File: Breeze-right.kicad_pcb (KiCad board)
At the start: 2 copper layers, 210.6 x 114.9 mm, 103 parts, among them J1 J, SW1 CHOCXHSPCB-1U, SW10 CHOCXHSPCB-1U, SW11 CHOCXHSPCB-1U, SW12 CHOCXHSPCB-1U, SW13 CHOCXHSPCB-1U, SW14 CHOCXHSPCB-1U, SW15 CHOCXHSPCB-1U, SW16 CHOCXHSPCB-1U, SW17 CHOCXHSPCB-1U, SW18 CHOCXHSPCB-1U, SW19 CHOCXHSPCB-1U, SW2 CHOCXHSPCB-1U, SW20 CHOCXHSPCB-1U, SW21 CHOCXHSPCB-1U, SW22 CHOCXHSPCB-1U, SW23 CHOCXHSPCB-1U, SW24 CHOCXHSPCB-1U, SW3 CHOCXHSPCB-1U, SW4 CHOCXHSPCB-1U, SW5 CHOCXHSPCB-1U, SW6 CHOCXHSPCB-1U, SW7 CHOCXHSPCB-1U, SW8 CHOCXHSPCB-1U, SW9 CHOCXHSPCB-1U

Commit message: done
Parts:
- removed H15: 2M-HOLE, Breeze:M2-HOLE
- removed H16, H17, H19: M3-HOLE, Breeze:M3-HOLE
- removed the H18 at (193.9, 114.4)
- removed MCU-MAIN1: PRO-MICRO, Breeze:ProMicro_1-Sided
- removed PWR1: SW_SPDT, Breeze:SS12D00
- added H12: M3, MountingHole:MountingHole_3.2mm_M3_ISO7380_Pad, F.Cu at (294.1, 120.3)
- added H14: M3, MountingHole:MountingHole_3.2mm_M3_ISO7380_Pad, F.Cu at (294.2, 158.2)
- added SW1: SW_SPDT, Breeze:SS12D00, F.Cu at (125.8, 167.5)
- added U1: NRF Supermini, Breeze:NRF_Supermini, B.Cu at (125.5, 134.5)
- D1, D2, D3, D4, D5, D6: value DIODE -> 1N4007W; footprint Breeze:SOD-123FL -> Breeze:SOD-123FL_L2.7-W1.8-LS3.7-RD
- D10: renamed from D7; value DIODE -> 1N4007W; footprint Breeze:SOD-123FL -> Breeze:SOD-123FL_L2.7-W1.8-LS3.7-RD
- D11: renamed from D8; value DIODE -> 1N4007W; footprint Breeze:SOD-123FL -> Breeze:SOD-123FL_L2.7-W1.8-LS3.7-RD
- D12: renamed from D9; value DIODE -> 1N4007W; footprint Breeze:SOD-123FL -> Breeze:SOD-123FL_L2.7-W1.8-LS3.7-RD
- D13: renamed from D10; value DIODE -> 1N4007W; footprint Breeze:SOD-123FL -> Breeze:SOD-123FL_L2.7-W1.8-LS3.7-RD
- D14: renamed from D11; value DIODE -> 1N4007W; footprint Breeze:SOD-123FL -> Breeze:SOD-123FL_L2.7-W1.8-LS3.7-RD
- D15: renamed from D12; value DIODE -> 1N4007W; footprint Breeze:SOD-123FL -> Breeze:SOD-123FL_L2.7-W1.8-LS3.7-RD
- D16: renamed from DMC4; value DIODE -> 1N4007W; footprint Breeze:SOD-123FL -> Breeze:SOD-123FL_L2.7-W1.8-LS3.7-RD
- D17: renamed from DMC5; value DIODE -> 1N4007W; footprint Breeze:SOD-123FL -> Breeze:SOD-123FL_L2.7-W1.8-LS3.7-RD
- D18: renamed from DMC6; value DIODE -> 1N4007W; footprint Breeze:SOD-123FL -> Breeze:SOD-123FL_L2.7-W1.8-LS3.7-RD
- D19: renamed from D13; value DIODE -> 1N4007W; footprint Breeze:SOD-123FL -> Breeze:SOD-123FL_L2.7-W1.8-LS3.7-RD
- D20: renamed from D14; value DIODE -> 1N4007W; footprint Breeze:SOD-123FL -> Breeze:SOD-123FL_L2.7-W1.8-LS3.7-RD
- D21: renamed from D15; value DIODE -> 1N4007W; footprint Breeze:SOD-123FL -> Breeze:SOD-123FL_L2.7-W1.8-LS3.7-RD
- D22: renamed from D16; value DIODE -> 1N4007W; footprint Breeze:SOD-123FL -> Breeze:SOD-123FL_L2.7-W1.8-LS3.7-RD
- D23: renamed from D17; value DIODE -> 1N4007W; footprint Breeze:SOD-123FL -> Breeze:SOD-123FL_L2.7-W1.8-LS3.7-RD
- D24: renamed from D18; value DIODE -> 1N4007W; footprint Breeze:SOD-123FL -> Breeze:SOD-123FL_L2.7-W1.8-LS3.7-RD
- D25: renamed from DUP1; value DIODE -> 1N4007W; footprint Breeze:SOD-123FL -> Breeze:SOD-123FL_L2.7-W1.8-LS3.7-RD
- D26: renamed from D19; value DIODE -> 1N4007W; footprint Breeze:SOD-123FL -> Breeze:SOD-123FL_L2.7-W1.8-LS3.7-RD
- D27: renamed from D20; value DIODE -> 1N4007W; footprint Breeze:SOD-123FL -> Breeze:SOD-123FL_L2.7-W1.8-LS3.7-RD
- D28: renamed from D21; value DIODE -> 1N4007W; footprint Breeze:SOD-123FL -> Breeze:SOD-123FL_L2.7-W1.8-LS3.7-RD
- D29: renamed from D22; value DIODE -> 1N4007W; footprint Breeze:SOD-123FL -> Breeze:SOD-123FL_L2.7-W1.8-LS3.7-RD
- D30: renamed from D23; value DIODE -> 1N4007W; footprint Breeze:SOD-123FL -> Breeze:SOD-123FL_L2.7-W1.8-LS3.7-RD
- D31: renamed from D24; value DIODE -> 1N4007W; footprint Breeze:SOD-123FL -> Breeze:SOD-123FL_L2.7-W1.8-LS3.7-RD
- D32: renamed from DALF1; value DIODE -> 1N4007W; footprint Breeze:SOD-123FL -> Breeze:SOD-123FL_L2.7-W1.8-LS3.7-RD
- D33: renamed from DAN1; value DIODE -> 1N4007W; footprint Breeze:SOD-123FL -> Breeze:SOD-123FL_L2.7-W1.8-LS3.7-RD
- D34: renamed from DRT1; value DIODE -> 1N4007W; footprint Breeze:SOD-123FL -> Breeze:SOD-123FL_L2.7-W1.8-LS3.7-RD
- D35: renamed from DTC1; value DIODE -> 1N4007W; footprint Breeze:SOD-123FL -> Breeze:SOD-123FL_L2.7-W1.8-LS3.7-RD
- D36: renamed from DTC2; value DIODE -> 1N4007W; footprint Breeze:SOD-123FL -> Breeze:SOD-123FL_L2.7-W1.8-LS3.7-RD
- D37: renamed from DTC3; value DIODE -> 1N4007W; footprint Breeze:SOD-123FL -> Breeze:SOD-123FL_L2.7-W1.8-LS3.7-RD
- D38: renamed from DTC4; value DIODE -> 1N4007W; footprint Breeze:SOD-123FL -> Breeze:SOD-123FL_L2.7-W1.8-LS3.7-RD
- D7: renamed from DMC1; value DIODE -> 1N4007W; footprint Breeze:SOD-123FL -> Breeze:SOD-123FL_L2.7-W1.8-LS3.7-RD
- D8: renamed from DMC2; value DIODE -> 1N4007W; footprint Breeze:SOD-123FL -> Breeze:SOD-123FL_L2.7-W1.8-LS3.7-RD
- D9: renamed from DMC3; value DIODE -> 1N4007W; footprint Breeze:SOD-123FL -> Breeze:SOD-123FL_L2.7-W1.8-LS3.7-RD
- H1, H10, H3, H4, H6, H7, H9: value M3-HOLE -> M3; footprint Breeze:M3-HOLE -> MountingHole:MountingHole_3.2mm_M3_ISO7380_Pad
- H11, H13: value 2M-HOLE -> M3; footprint Breeze:M2-HOLE -> MountingHole:MountingHole_3.2mm_M3_ISO7380_Pad
- H2, H5, H8: value M3-HOLE -> M3; footprint Breeze:M3-HOLE -> MountingHole:MountingHole_3.2mm_M3_ISO7380_Pad_TopOnly
- J1: value J -> Conn_01x02
- moved H10 153.2 mm to (142.5, 179.6)
- moved H1 121.4 mm to (155.9, 116.2)
- moved H9 92.1 mm to (232.1, 158.2)
- moved H4 79.5 mm to (155.9, 135.4)
- moved H8 41.6 mm to (193.9, 152.4)
- moved H6 40.4 mm to (232.1, 139.1)
- moved H2 38.0 mm to (193.9, 114.4)
- moved H11 29.6 mm to (275.0, 120.1)
- moved H13 22.5 mm to (275.1, 139.2)
- moved H3 19.1 mm to (232.1, 120.0)
- moved D5 8.34 mm to (212.0, 110.8)
- moved D29 8.14 mm to (193.0, 163.2)
- moved D14 8.07 mm to (212.0, 130.0)
- moved D23 7.88 mm to (212.0, 149.2)
- moved D12 7.18 mm to (174.0, 123.8)
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- renumbered LGO1 to G1, STABL1 to H18, J_RIGHT1 to J2, J_FUNCT1 to J3, J_RIGHT2 to J4, J_FUNCT2 to J5, RST1 to SW2, UP1 to UPXS1, SW1 to XS1, SW7 to XS10, SW8 to XS11, SW9 to XS12, SW10 to XS13, SW11 to XS14, SW12 to XS15, MC4 to XS16, MC5 to XS17, MC6 to XS18, SW13 to XS19, SW2 to XS2, SW14 to XS20, SW15 to XS21, SW16 to XS22, SW17 to XS23, SW18 to XS24, SW19 to XS25, SW20 to XS26, SW21 to XS27, SW22 to XS28, SW23 to XS29, SW3 to XS3, SW24 to XS30, LEFT1 to XS31, DOWN1 to XS32, RIGHT1 to XS33, TC1 to XS34, TC2 to XS35, TC3 to XS36, TC4 to XS37, SW4 to XS4, SW5 to XS5, SW6 to XS6, MC1 to XS7, MC2 to XS8, MC3 to XS9
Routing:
- net ROW3: track 327.6 -> 257.2 mm, vias 17 -> 2
- net BAT_PLUS: track 49.5 -> 0.00 mm
- net +BATT: track 0.00 -> 48.7 mm, vias 0 -> 2
- net COL6: track 301.7 -> 264.1 mm, vias 7 -> 6
- net COL1: track 183.6 -> 147.6 mm, vias 1 -> 9
- net COL7: track 292.8 -> 259.7 mm, vias 8 -> 6
- net COL0: track 173.1 -> 150.5 mm, vias 1 -> 9
- net ROW4: track 122.1 -> 103.3 mm, vias 6 -> 0
- net COL8: track 311.9 -> 293.5 mm, vias 7 -> 4
- net COL2: track 183.4 -> 167.9 mm, vias 3 -> 8
- net ROW2: track 222.9 -> 208.4 mm, vias 12 -> 2
- net GND: track 14.3 -> 0.00 mm, vias 26 -> 98
- net COL5: track 217.4 -> 203.1 mm, vias 1 -> 3
- net ROW0: track 244.1 -> 257.6 mm, vias 12 -> 0
- net COL3: track 196.8 -> 188.1 mm, vias 1 -> 7
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
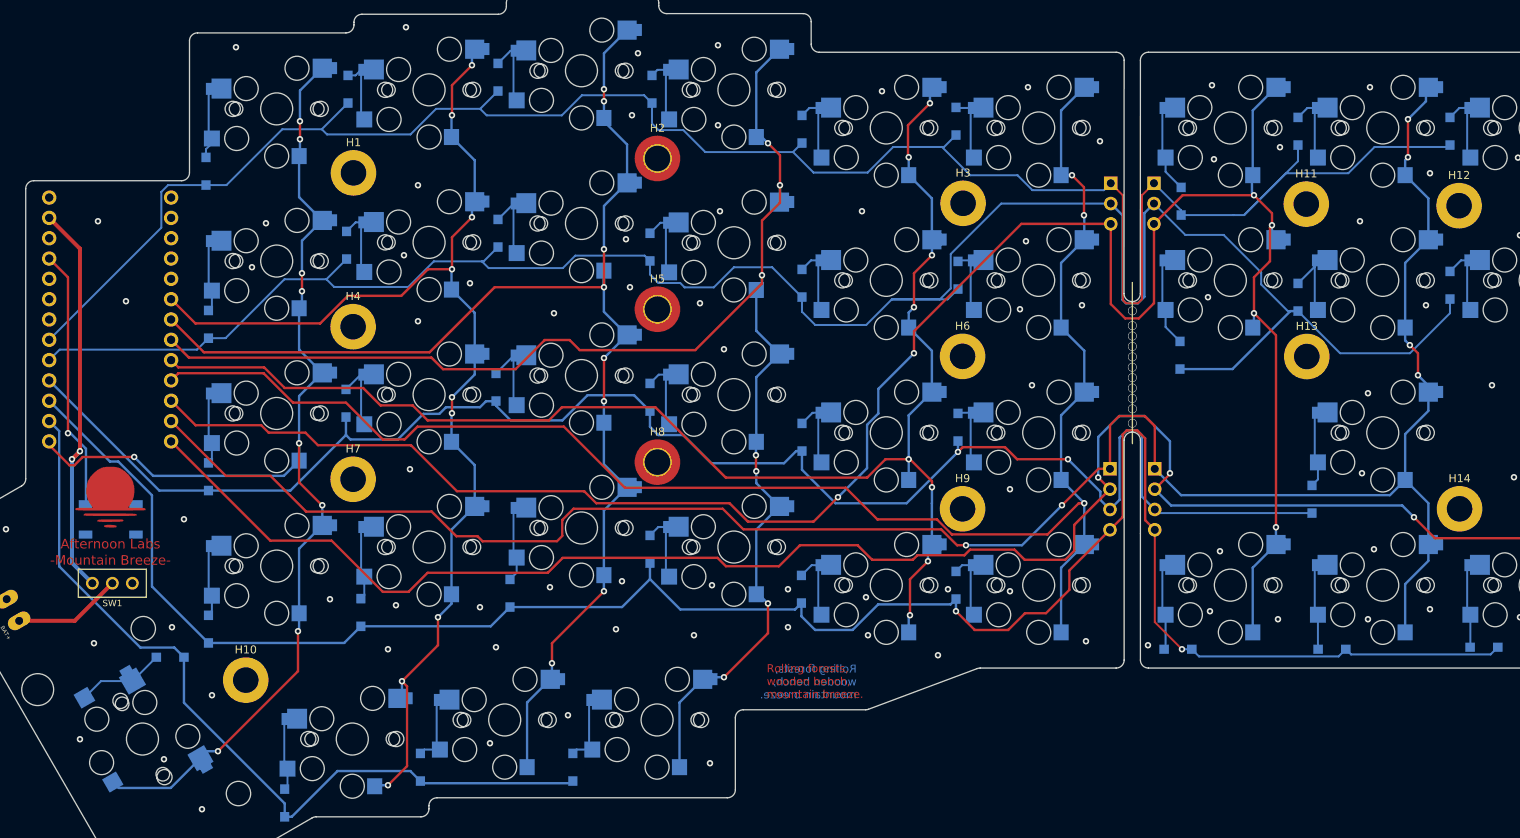
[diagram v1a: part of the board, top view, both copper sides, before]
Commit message: trace width parity, correct arduino mounting side
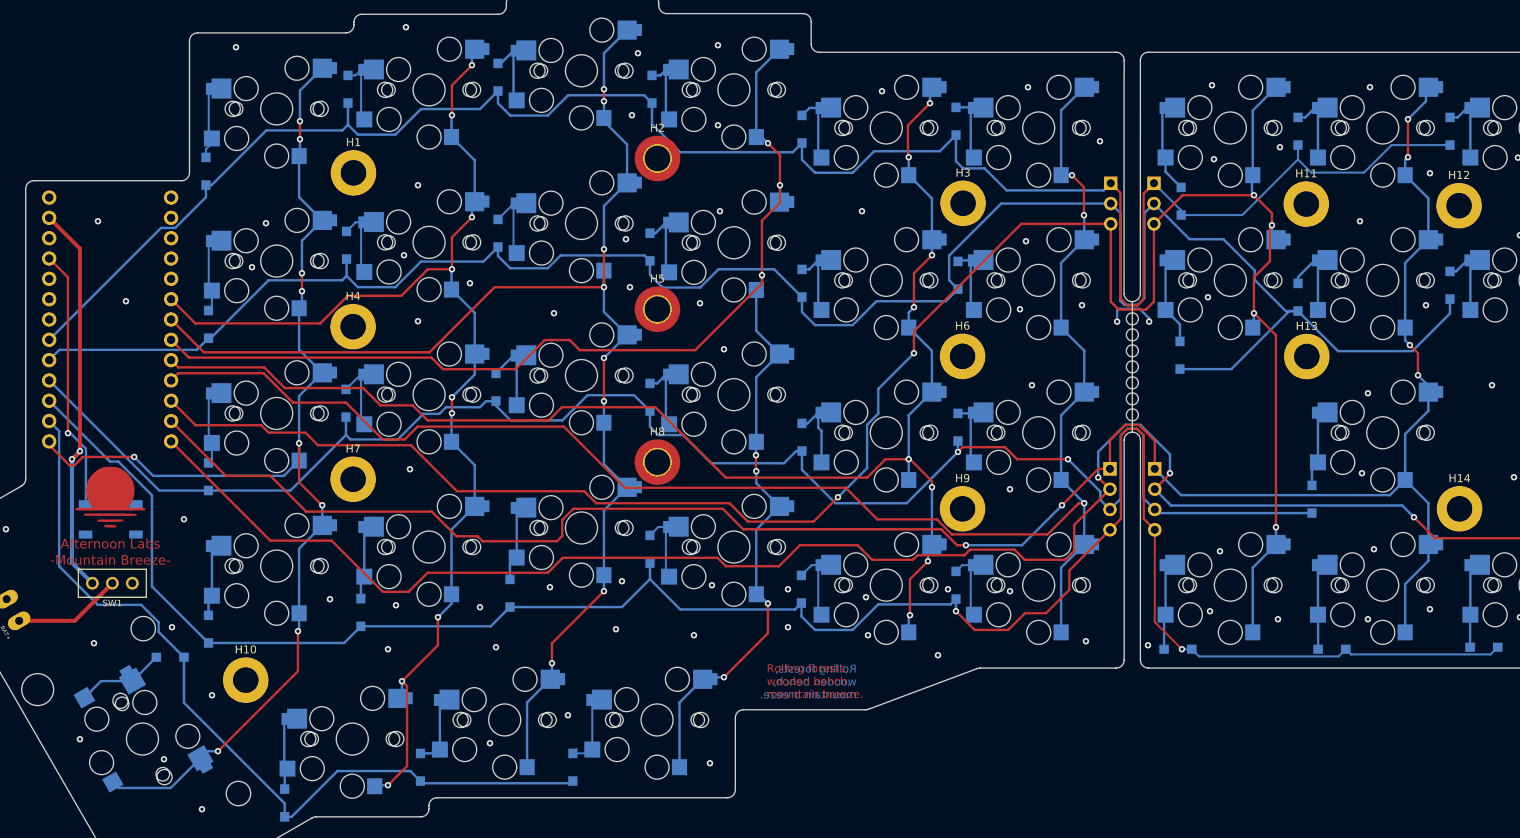
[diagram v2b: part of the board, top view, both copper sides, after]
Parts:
- added REF**: mouse bites, Breeze:mousebites, F.Cu at (253.3, 140.4)
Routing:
- net ROW0: track 257.6 -> 247.5 mm
- net ROW1: track 266.5 -> 257.6 mm
- net GND: track 0.00 -> 6.58 mm, vias 98 -> 89
- net COL7: track 259.7 -> 255.3 mm
- net COL8: track 293.5 -> 290.5 mm
- net COL6: track 264.1 -> 261.9 mm
- net COL3: track 188.1 -> 186.0 mm
- net COL1: track 147.6 -> 145.8 mm
- net Net-(D1-A): track 9.04 -> 7.87 mm
- net Net-(D10-A): track 9.02 -> 7.85 mm
- net Net-(D19-A): track 9.02 -> 7.85 mm
- net COL0: track 150.5 -> 149.4 mm
- net COL4: track 179.9 -> 178.9 mm
- net COL2: track 167.9 -> 167.1 mm
- net Net-(D15-A): track 8.01 -> 7.26 mm
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
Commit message: fix mis-named component(xs25)
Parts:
- renumbered UPXS1 to XS25, XS25 to XS26, XS26 to XS27, XS27 to XS28, XS28 to XS29, XS29 to XS30, XS30 to XS31, XS31 to XS32, XS32 to XS33, XS33 to XS34, XS34 to XS35, XS35 to XS36, XS36 to XS37, XS37 to XS38
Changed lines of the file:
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@@
 		(layer "B.Cu")
 		(at 284.598 167.74 180)
-		(property "Reference" "XS32"
+		(property "Reference" "XS33"
 			(at -4 -2 0)
 			(layer "B.SilkS")
@@
 		(layer "B.Cu")
 		(at 265.548 167.74 180)
-		(property "Reference" "XS31"
+		(property "Reference" "XS32"
 			(at -4 -2 0)
 			(layer "B.SilkS")
@@
 		(layer "B.Cu")
 		(at 303.648 167.74 180)
-		(property "Reference" "XS33"
+		(property "Reference" "XS34"
 			(at -4 -2 0)
 			(layer "B.SilkS")
@@
 		(layer "B.Cu")
 		(at 284.598 148.69 180)
-		(property "Reference" "UPXS1"
+		(property "Reference" "XS25"
 			(at -4 -2 0)
 			(layer "B.SilkS")
@@
 		(layer "B.Cu")
 		(at 146.34 165.356 180)
-		(property "Reference" "XS25"
+		(property "Reference" "XS26"
 			(at -4 -2 0)
 			(layer "B.SilkS")
@@
 		(layer "B.Cu")
 		(at 165.39 162.975 180)
-		(property "Reference" "XS26"
+		(property "Reference" "XS27"
 			(at -4 -2 0)
 			(layer "B.SilkS")
@@
 		(layer "B.Cu")
 		(at 184.44 160.59 180)
-		(property "Reference" "XS27"
+		(property "Reference" "XS28"
 			(at -4 -2 0)
 			(layer "B.SilkS")
@@
 		(layer "B.Cu")
 		(at 203.49 162.975 180)
-		(property "Reference" "XS28"
+		(property "Reference" "XS29"
 			(at -4 -2 0)
 			(layer "B.SilkS")
@@
 		(layer "B.Cu")
 		(at 222.54 167.74 180)
-		(property "Reference" "XS29"
+		(property "Reference" "XS30"
 			(at -4 -2 0)
 			(layer "B.SilkS")
@@
 		(layer "B.Cu")
 		(at 241.59 167.74 180)
-		(property "Reference" "XS30"
+		(property "Reference" "XS31"
 			(at -4 -2 0)
 			(layer "B.SilkS")
@@
 		(layer "B.Cu")
 		(at 129.563 186.974 120)
-		(property "Reference" "XS34"
+		(property "Reference" "XS35"
 			(at -4 -2 300)
 			(layer "B.SilkS")
@@
 		(layer "B.Cu")
 		(at 155.79 186.974 180)
-		(property "Reference" "XS35"
+		(property "Reference" "XS36"
 			(at -4 -2 0)
 			(layer "B.SilkS")
@@
 		(layer "B.Cu")
 		(at 174.84 184.59 180)
-		(property "Reference" "XS36"
+		(property "Reference" "XS37"
 			(at -4 -2 0)
 			(layer "B.SilkS")
@@
 		(layer "B.Cu")
 		(at 193.89 184.59 180)
-		(property "Reference" "XS37"
+		(property "Reference" "XS38"
 			(at -4 -2 0)
 			(layer "B.SilkS")
